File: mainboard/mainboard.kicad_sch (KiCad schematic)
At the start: 52 parts, among them J1 Servo, J2 ADC Pins, J3 USB Data, J4 Button Interface, J5 Power, J6 Release Button, J7 GPIO Pins, Q1 BSS138, SW1 SW_Push, U1 RP2040, U2 W25Q128JVS, U3 RV-3028-C7, U4 ITR9608-F, Y1 Crystal_ABM8

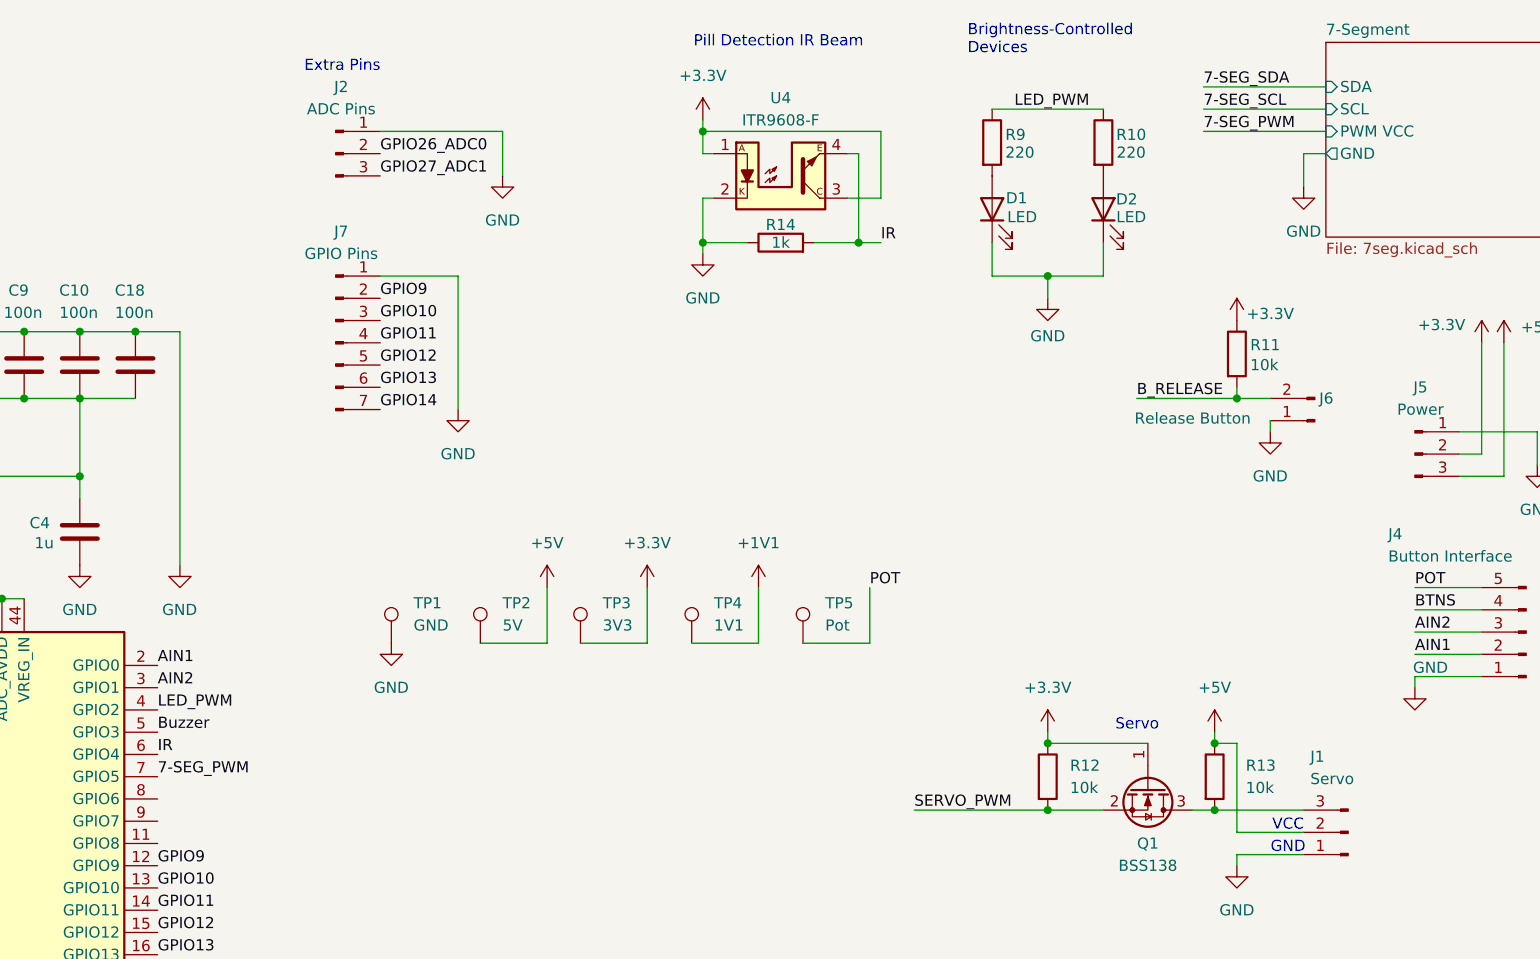
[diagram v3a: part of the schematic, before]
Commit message: 7-seg changes & wire reroutes
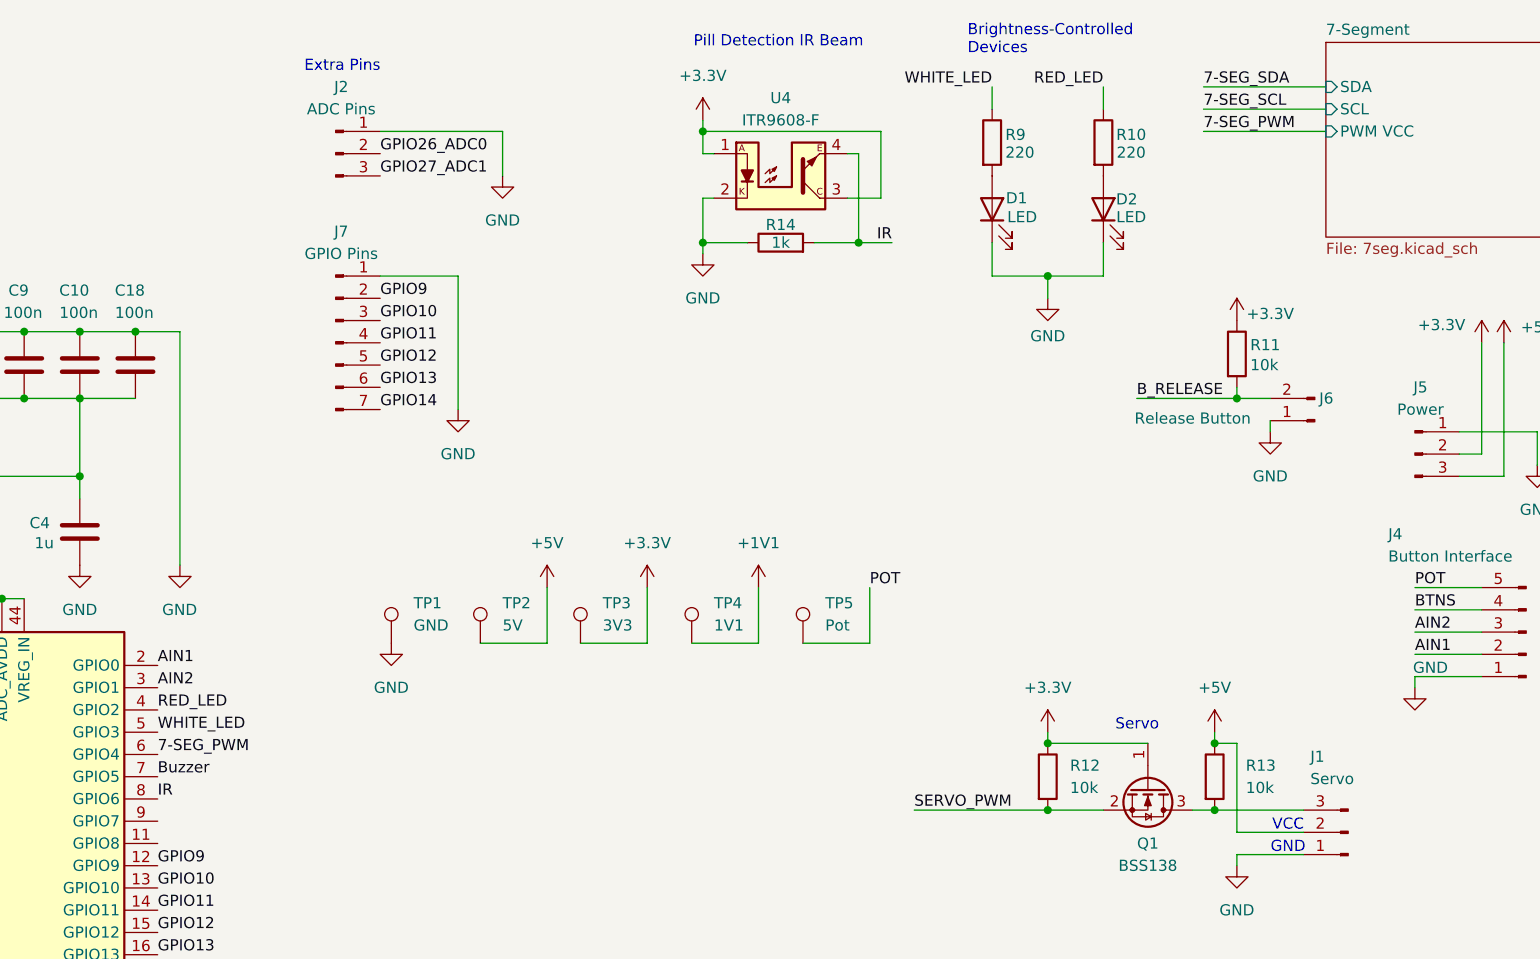
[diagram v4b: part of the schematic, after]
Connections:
- net 7-SEG_PWM: now also U1.6 (GPIO4); no longer U1.7 (GPIO5)
- net Buzzer: now also U1.7 (GPIO5); no longer U1.5 (GPIO3)
- net IR: now also U1.8 (GPIO6); no longer U1.6 (GPIO4)
- net LED_PWM renamed RED_LED
- net RED_LED: no longer R9.1
- new net WHITE_LED: R9.1, U1.5 (GPIO3)
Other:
- sheet 7-Segment ports: added none; removed GND
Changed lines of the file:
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@@
 	(wire
 		(pts
-			(xy 219.71 24.13) (xy 232.41 24.13)
-		)
-		(stroke
-			(width 0)
-			(type default)
-		)
-	)
-	(wire
-		(pts
 			(xy 259.08 143.51) (xy 259.08 138.43)
 		)
@@
 	(wire
 		(pts
+			(xy 232.41 21.59) (xy 232.41 24.13)
+		)
+		(stroke
+			(width 0)
+			(type default)
+		)
+	)
+	(wire
+		(pts
 			(xy 204.47 29.21) (xy 204.47 39.37)
 		)
@@
 	(wire
 		(pts
+			(xy 219.71 21.59) (xy 219.71 24.13)
+		)
+		(stroke
+			(width 0)
+			(type default)
+		)
+	)
+	(wire
+		(pts
 			(xy 251.46 143.51) (xy 259.08 143.51)
 		)
@@
 	(wire
 		(pts
-			(xy 255.27 33.02) (xy 255.27 29.21)
-		)
-		(stroke
-			(width 0)
-			(type default)
-		)
-	)
-	(wire
-		(pts
 			(xy 62.23 105.41) (xy 73.66 105.41)
 		)
@@
 	(wire
 		(pts
-			(xy 204.47 39.37) (xy 207.01 39.37)
+			(xy 204.47 39.37) (xy 208.28 39.37)
 		)
 		(stroke
@@
 	(wire
 		(pts
-			(xy 255.27 29.21) (xy 257.81 29.21)
-		)
-		(stroke
-			(width 0)
-			(type default)
-		)
-	)
-	(wire
-		(pts
 			(xy 20.32 133.35) (xy 20.32 143.51)
 		)
@@
 	)
 	(label "IR"
-		(at 207.01 39.37 0)
+		(at 208.28 39.37 180)
 		(effects
 			(font
 				(size 1.27 1.27)
 			)
-			(justify left bottom)
+			(justify right bottom)
 		)
 	)
@@
 		)
 	)
-	(label "LED_PWM"
+	(label "RED_LED"
 		(at 124.46 92.71 0)
 		(effects
@@
 		)
 	)
+	(label "WHITE_LED"
+		(at 219.71 21.59 180)
+		(effects
+			(font
+				(size 1.27 1.27)
+			)
+			(justify right bottom)
+		)
+	)
 	(label "Buzzer"
+		(at 124.46 100.33 0)
+		(effects
+			(font
+				(size 1.27 1.27)
+			)
+			(justify left bottom)
+		)
+	)
+	(label "WHITE_LED"
 		(at 124.46 95.25 0)
 		(effects
@@
 	)
 	(label "IR"
-		(at 124.46 97.79 0)
+		(at 124.46 102.87 0)
 		(effects
 			(font
@@
 	)
 	(label "7-SEG_PWM"
-		(at 124.46 100.33 0)
+		(at 124.46 97.79 0)
 		(effects
 			(font
@@
 		)
 	)
-	(label "AIN2"
-		(at 124.46 90.17 0)
+	(label "RED_LED"
+		(at 232.41 21.59 180)
 		(effects
 			(font
 				(size 1.27 1.27)
 			)
-			(justify left bottom)
+			(justify right bottom)
 		)
 	)
-	(label "LED_PWM"
-		(at 222.25 24.13 0)
+	(label "AIN2"
+		(at 124.46 90.17 0)
 		(effects
 			(font
@@
 	)
 	(symbol
-		(lib_id "power:GND")
-		(at 255.27 33.02 0)
-		(unit 1)
-		(exclude_from_sim no)
-		(in_bom yes)
-		(on_board yes)
-		(dnp no)
-		(fields_autoplaced yes)
-		(property "Reference" "#PWR09"
-			(at 255.27 39.37 0)
-			(effects
-				(font
-					(size 1.27 1.27)
-				)
-				(hide yes)
-			)
-		)
-		(property "Value" "GND"
-			(at 255.27 38.1 0)
-			(effects
-				(font
-					(size 1.27 1.27)
-				)
-			)
-		)
-		(property "Footprint" ""
-			(at 255.27 33.02 0)
-			(effects
-				(font
-					(size 1.27 1.27)
-				)
-				(hide yes)
-			)
-		)
-		(property "Datasheet" ""
-			(at 255.27 33.02 0)
-			(effects
-				(font
-					(size 1.27 1.27)
-				)
-				(hide yes)
-			)
-		)
-		(property "Description" "Power symbol creates a global label with name \"GND\" , ground"
-			(at 255.27 33.02 0)
-			(effects
-				(font
-					(size 1.27 1.27)
-				)
-				(hide yes)
-			)
-		)
-		(pin "1"
-		)
-		(instances
-			(project ""
-				(path "/57f2b6ac-3611-4b16-b8a1-8e91b00e0208"
-					(reference "#PWR09")
-					(unit 1)
-				)
-			)
-		)
-	)
-	(symbol
 		(lib_id "Device:LED")
 		(at 219.71 35.56 90)
@@
 			)
 		)
-		(pin "GND" output
-			(at 257.81 29.21 180)
-			(effects
-				(font
-					(size 1.27 1.27)
-				)
-				(justify left)
-			)
-		)

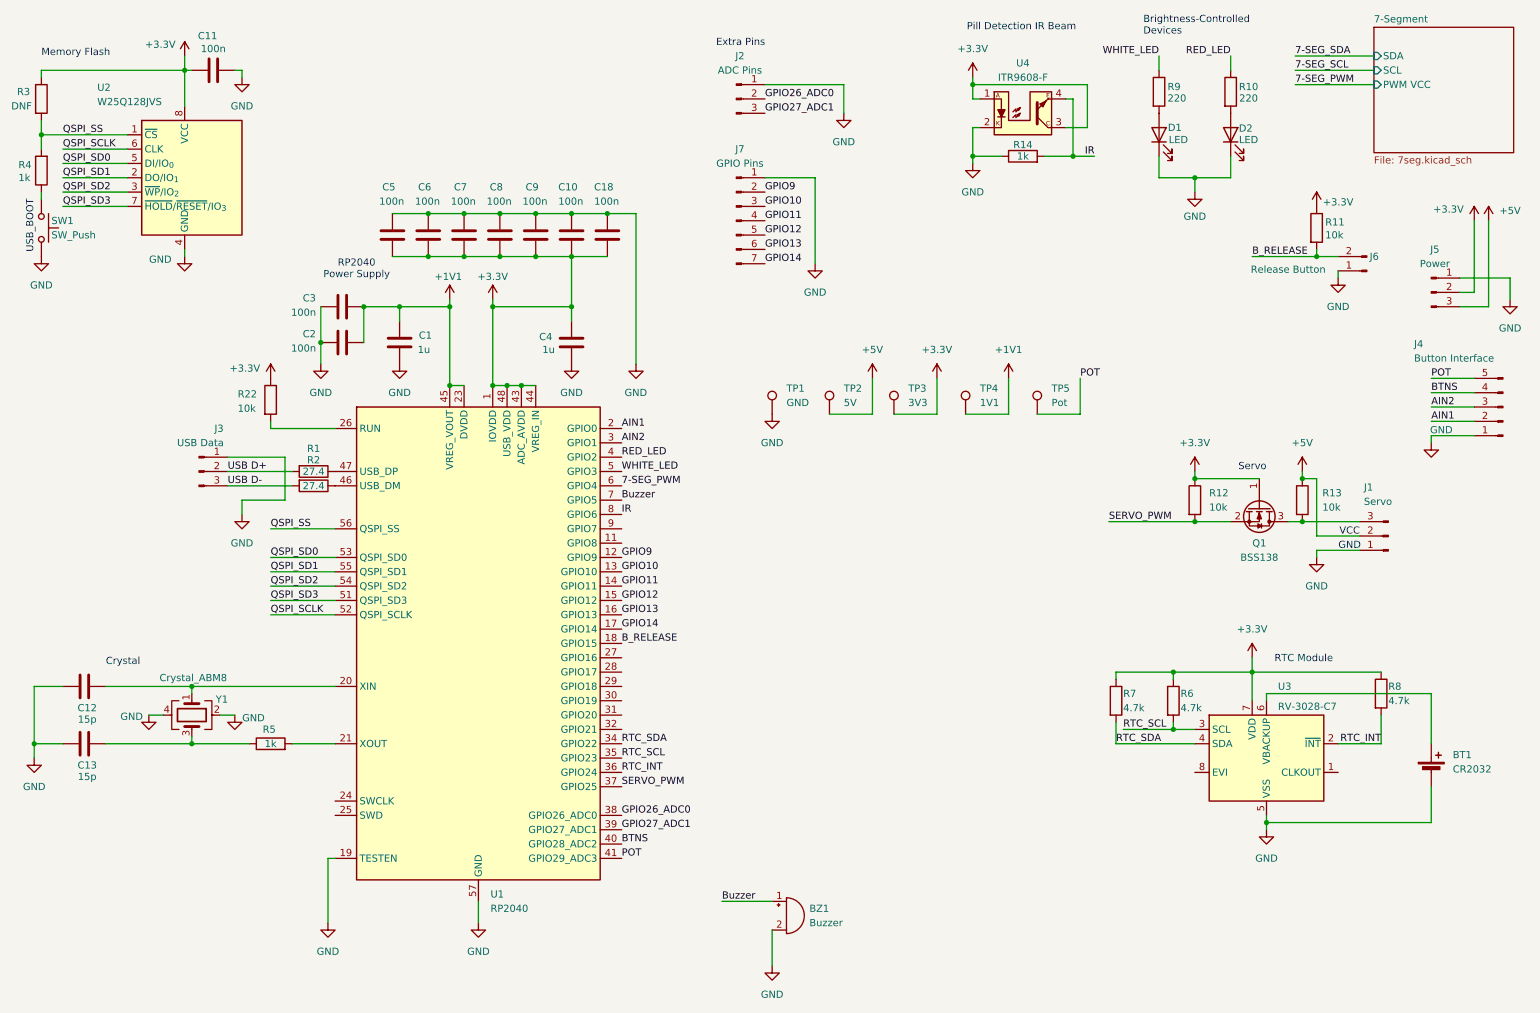
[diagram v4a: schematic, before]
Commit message: Swtiched connectors to Clik-MATE.
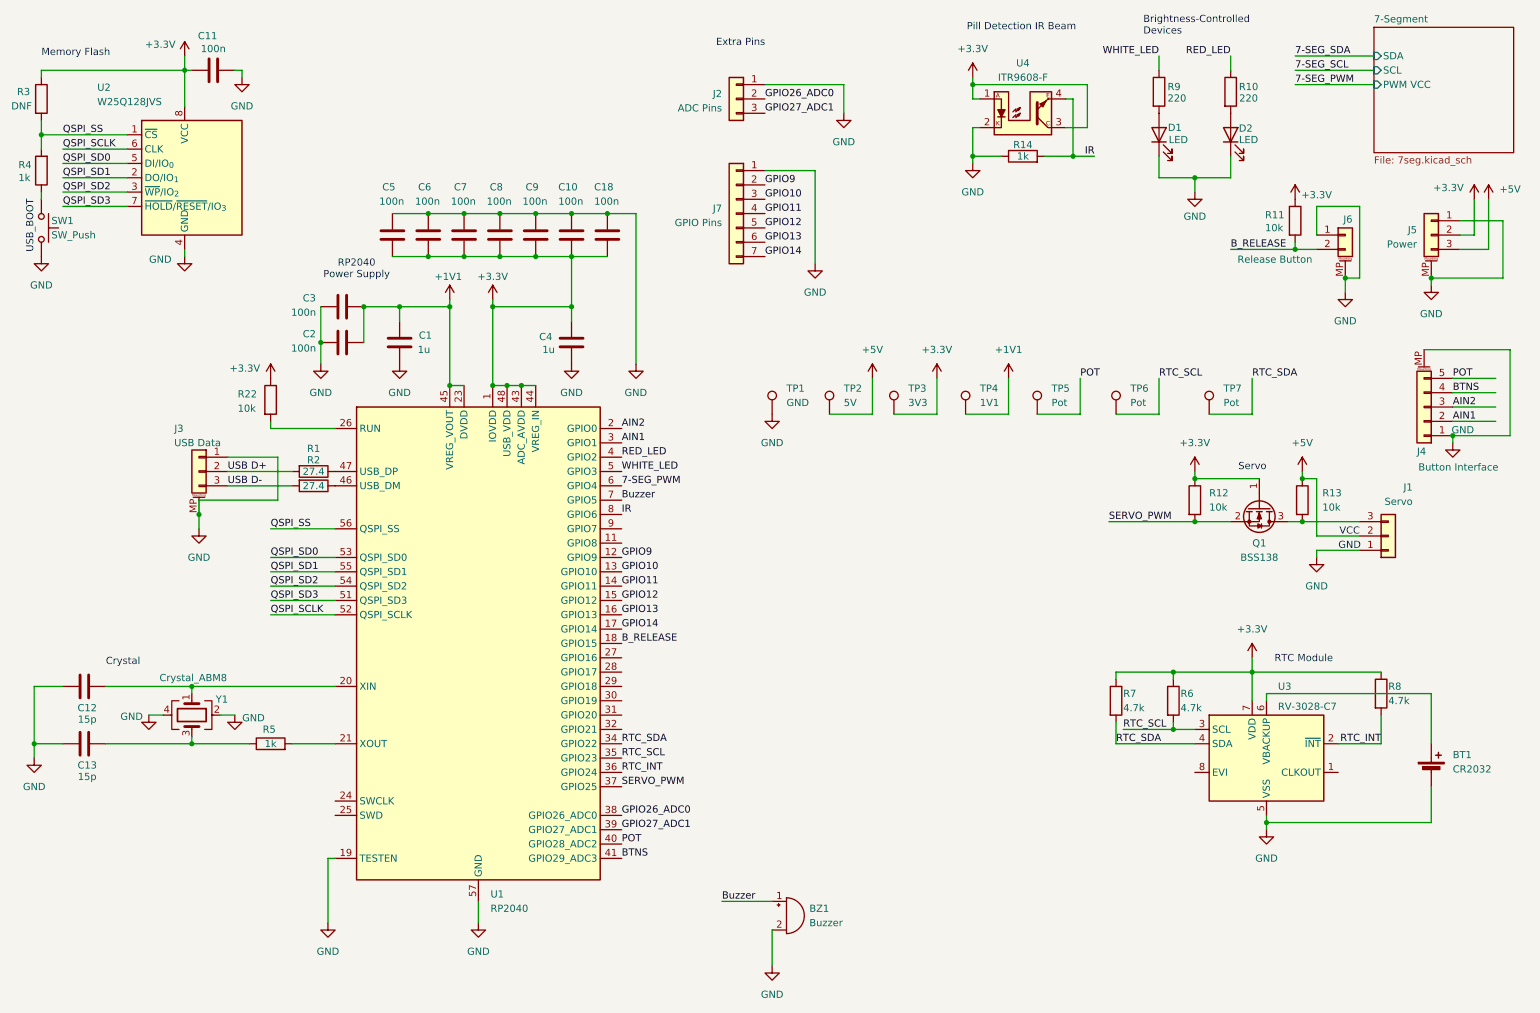
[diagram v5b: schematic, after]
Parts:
- added TP6, TP7: Pot, TestPoint:TestPoint_Pad_D1.5mm, symbol Connector:TestPoint
- J1, J2: symbol Connector:Conn_01x03_Pin -> Connector_Generic:Conn_01x03
- J3, J5: footprint Connector_JST:JST_EH_B3B-EH-A_1x03_P2.50mm_Vertical -> Connector_Molex:Molex_CLIK-Mate_505405-0370_1x03-1MP_P1.50mm_Vertical; symbol Connector:Conn_01x03_Pin -> Connector_Generic_MountingPin:Conn_01x03_MountingPin
- J4: footprint Connector_JST:JST_EH_B5B-EH-A_1x05_P2.50mm_Vertical -> Connector_Molex:Molex_CLIK-Mate_505405-0570_1x05-1MP_P1.50mm_Vertical; symbol Connector:Conn_01x05_Pin -> Connector_Generic_MountingPin:Conn_01x05_MountingPin
- J6: footprint Connector_JST:JST_EH_B2B-EH-A_1x02_P2.50mm_Vertical -> Connector_Molex:Molex_CLIK-Mate_505405-0270_1x02-1MP_P1.50mm_Vertical; symbol Connector:Conn_01x02_Pin -> Connector_Generic_MountingPin:Conn_01x02_MountingPin
- J7: symbol Connector:Conn_01x07_Pin -> Connector_Generic:Conn_01x07
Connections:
- net AIN1: now also U1.3 (GPIO1); no longer U1.2 (GPIO0)
- net AIN2: now also U1.2 (GPIO0); no longer U1.3 (GPIO1)
- net BTNS: now also U1.41 (GPIO29_ADC3); no longer U1.40 (GPIO28_ADC2)
- net GND: now also J3.MP (MountPin), J4.MP (MountPin), J5.MP (MountPin), J6.MP (MountPin)
- net POT: now also U1.40 (GPIO28_ADC2); no longer U1.41 (GPIO29_ADC3)
- net RTC_SCL: now also TP6.1
- net RTC_SDA: now also TP7.1
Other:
- moved on the sheet: J3, J5, R11
